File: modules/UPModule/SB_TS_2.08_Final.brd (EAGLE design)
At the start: 42.3 x 27.4 mm, 68 parts, among them IC1 MC34063AD, IC2 MCP1702-33, IC3 LPC922FDH, Q1 BC856, Q2 BCP52, Q4 ASFL, T1 BC848, T2 BC848

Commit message: first upload TS-ARM3.05
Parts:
- moved L1 0.19 mm to (27.0, 5.64)
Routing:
- net PROG: track 15.8 -> 15.6 mm, vias 0 -> 1

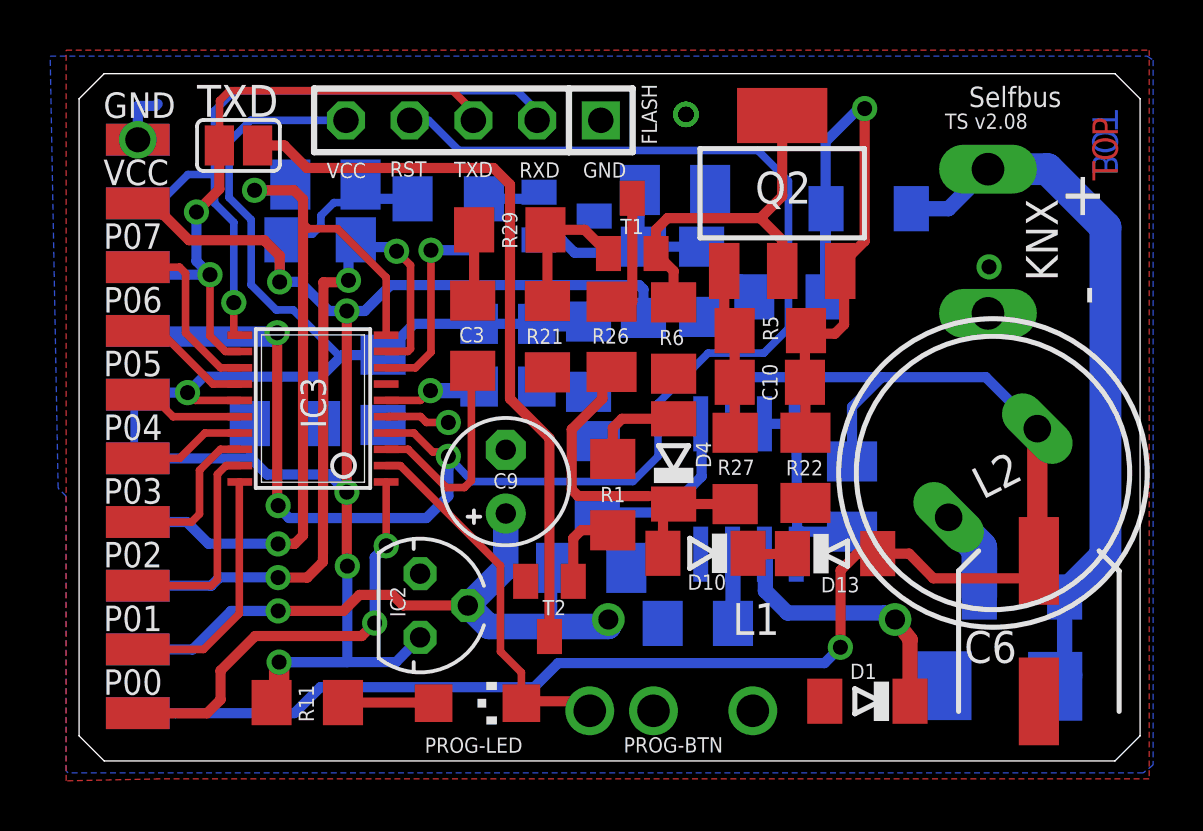
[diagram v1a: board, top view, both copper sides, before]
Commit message: text placement optimized; missing values added
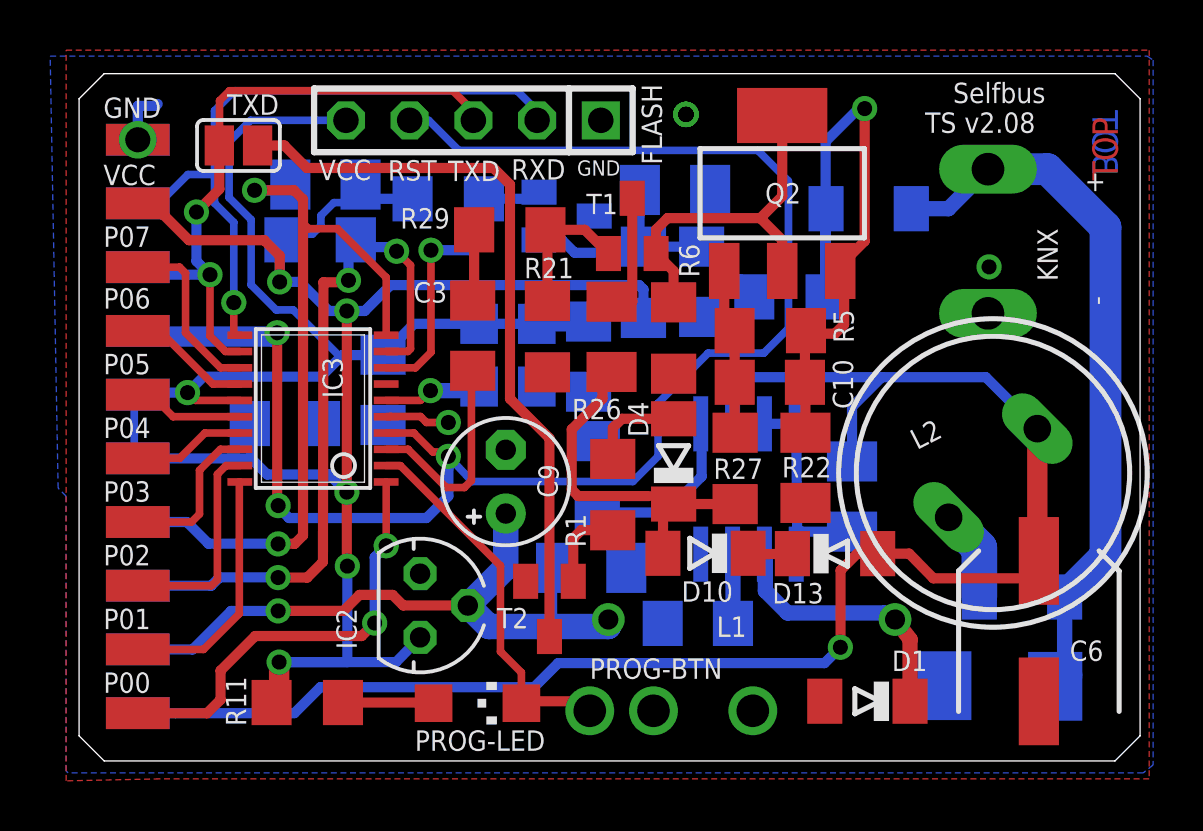
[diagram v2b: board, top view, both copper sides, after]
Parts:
- C7: value (none) -> 100n
- C8: value 10nf -> 10n
- C9: value (none) -> 100µ / 6.3V
